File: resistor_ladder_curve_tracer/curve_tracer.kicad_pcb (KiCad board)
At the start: 2 copper layers, 50.2 x 49.3 mm, 46 parts, among them J1 Screw_Terminal_01x04, J2 Conn_01x10_Female, J3 Conn_01x10_Female, U1 INA180B2IDBVT, U10 ADG841YKSZ-500RL7, U11 ADG841YKSZ-500RL7, U12 ADG841YKSZ-500RL7, U13 ADG841YKSZ-500RL7, U2 MCP6401RT-xOT, U4 AP2112K-3.3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

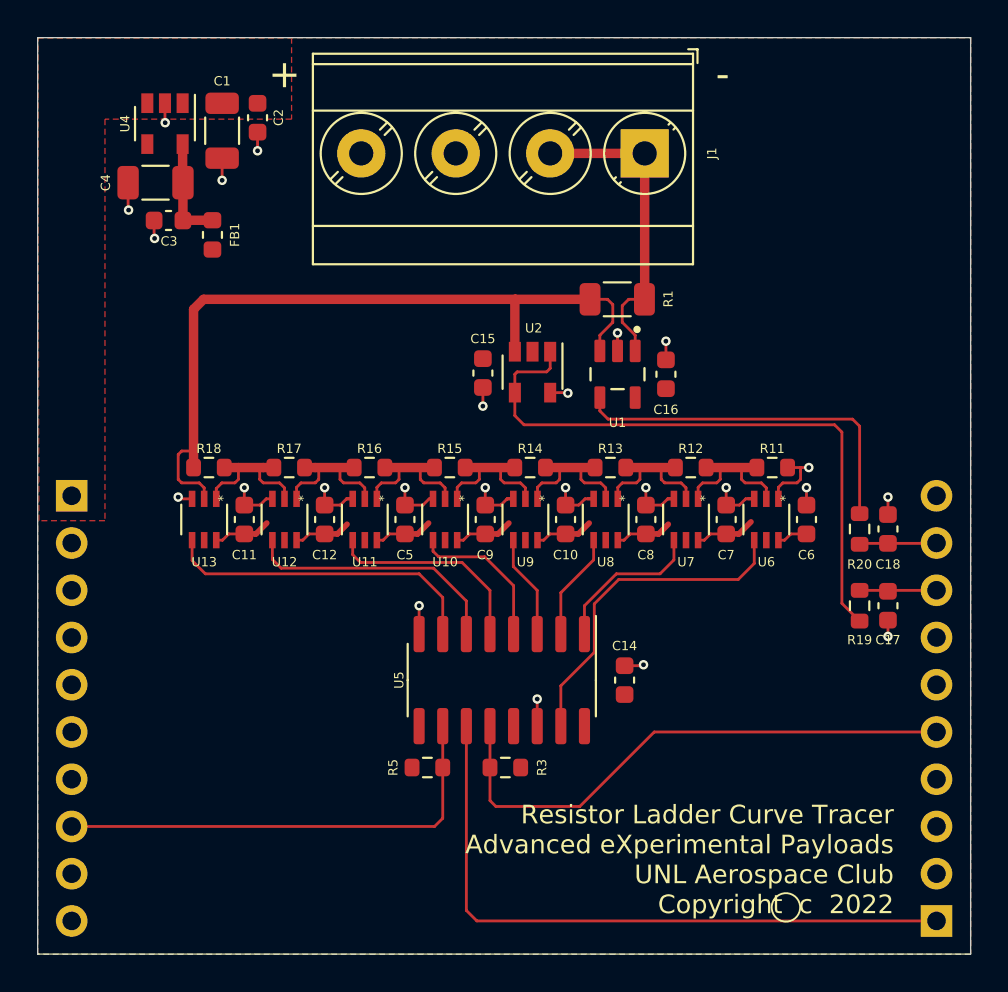
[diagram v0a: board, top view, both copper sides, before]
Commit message: Update boards
- Added flight computer board outline
- Added GUI for curve tracer
- Updated curve tracer
- Updated perovskite switcher
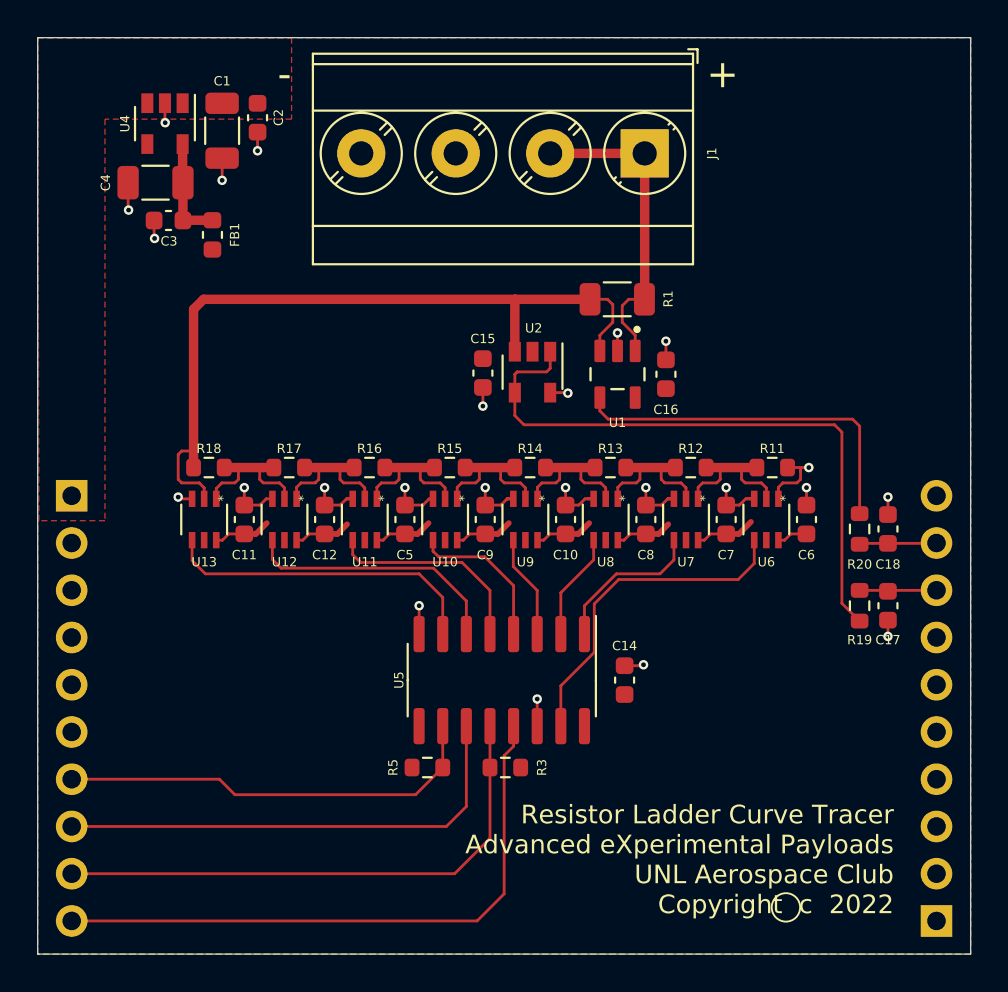
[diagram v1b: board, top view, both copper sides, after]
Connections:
- net ANALOG_PWR_EN renamed Net-(J2-Pad5)
- J2 pad 10: Net-(J2-Pad10) -> LADDER_LATCH
- J2 pad 7: Net-(J2-Pad7) -> LADDER_RESET
- J2 pad 8: LADDER_RESET -> LADDER_CLOCK
- J2 pad 9: Net-(J2-Pad9) -> LADDER_EN
- J3 pad 1: LADDER_CLOCK -> Net-(J3-Pad1)
- J3 pad 5: LADDER_EN -> Net-(J3-Pad5)
- U5 pad 13: Net-(U5-Pad13) -> LADDER_LATCH
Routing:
- net LADDER_LATCH: track 0.00 -> 33.1 mm
- net LADDER_CLOCK: track 35.4 -> 26.0 mm
- net LADDER_RESET: track 25.1 -> 23.1 mm

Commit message: Working on flight computer
- Update resistor ladder curve tracer silkscreen, schematic, and layout
- Flight computer schematic drafted for MSP430 circuits, updated curve tracer, perovskite switching network.
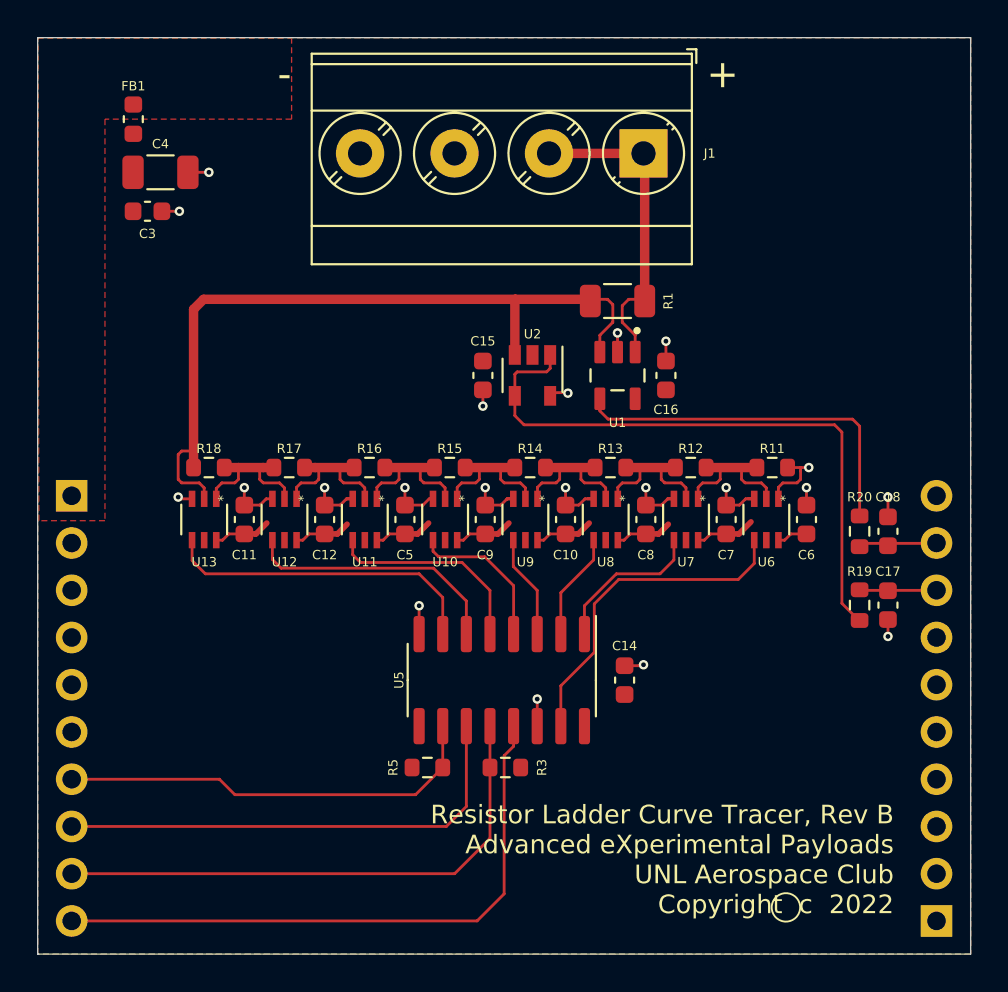
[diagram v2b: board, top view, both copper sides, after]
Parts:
- removed C1: 10u, Capacitor_SMD:C_1206_3216Metric
- removed C2: 1u, Capacitor_SMD:C_0603_1608Metric
- removed U4: AP2112K-3.3, Package_TO_SOT_SMD:SOT-23-5
- moved FB1 7.54 mm to (129.6, 88.8), turned to 270 degrees
- moved C3 1.23 mm to (130.4, 93.8), turned to 0 degrees
- moved C4 0.62 mm to (131.1, 91.7), turned to 0 degrees
- moved U2 0.18 mm to (151.1, 102.6)
- moved C15 0.13 mm to (148.4, 102.6)
- moved C18 0.13 mm to (170.2, 111.0)
- moved R20 0.13 mm to (168.7, 111.0)
- moved R1 0.09 mm to (155.6, 98.6)
- moved C16 0.06 mm to (158.2, 102.6)
- moved U1 0.06 mm to (155.6, 102.6)
- moved J1 0.06 mm to (157.0, 90.7)
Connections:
- net /Resistor Ladder/V_PANEL renamed /Panel Measurements/V_PANEL
- C3 pad 1: Net-(C3-Pad1) -> +3V3
- C4 pad 1: Net-(C3-Pad1) -> +3V3
- FB1 pad 1: +3V3 -> Net-(FB1-Pad1)
- FB1 pad 2: Net-(C3-Pad1) -> +3V3
- J2 pad 1: VBUS -> Net-(FB1-Pad1)
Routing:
- net Net-(C3-Pad1): track 5.71 -> 0.00 mm
- net GND: track 40.8 -> 37.1 mm, vias 24 -> 21
- added copper zone on F.Cu, net Net-(FB1-Pad1)
- removed copper zone on F.Cu, net VBUS
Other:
- board text added: "Resistor Ladder Curve Tracer, Rev B Advanced eXperimental Payloads UNL Aerospace Club Copyright c 2022"
- board text removed: "Resistor Ladder Curve Tracer Advanced eXperimental Payloads UNL Aerospace Club Copyright c 2022"

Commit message: Working on NREL pieces
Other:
- board text added: "Resistor Ladder Curve Tracer, Rev C Advanced eXperimental Payloads UNL Aerospace Club Copyright c 2022"
- board text removed: "Resistor Ladder Curve Tracer, Rev B Advanced eXperimental Payloads UNL Aerospace Club Copyright c 2022"
